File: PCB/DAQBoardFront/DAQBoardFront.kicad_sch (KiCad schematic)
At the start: 42 parts, among them IC2 LMR51430YDDCR, J2 53375-0410, U5 TCAN1051VDRQ1

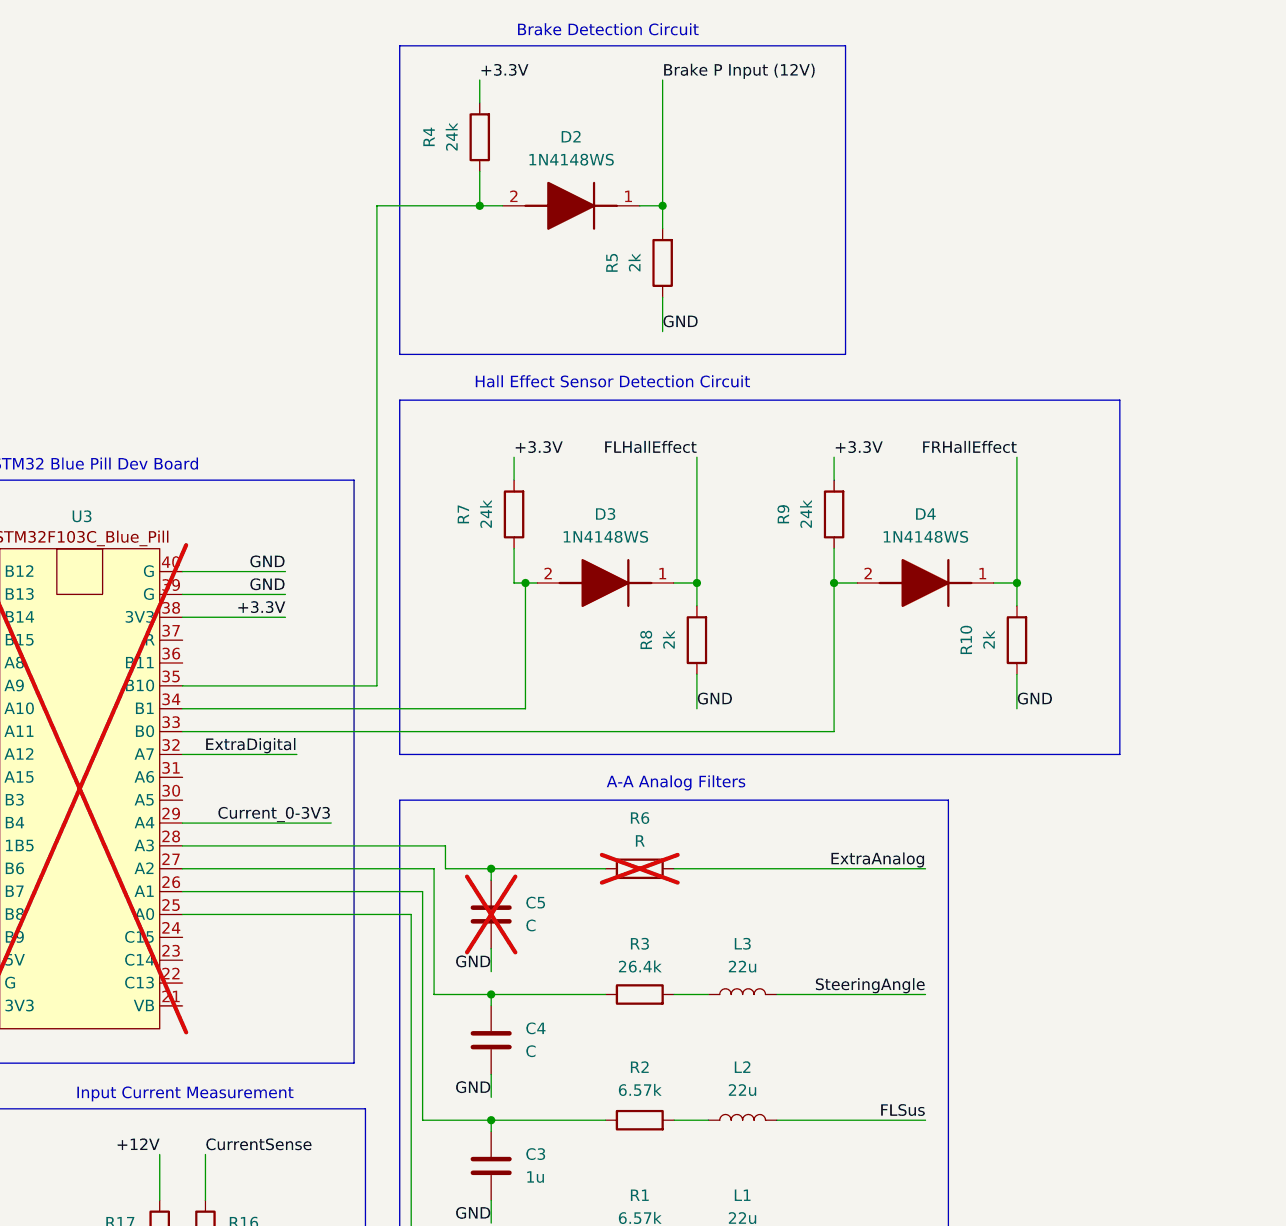
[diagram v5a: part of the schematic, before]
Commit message: Created hall effect test script for T4.1, adjusted hall effect input strategy
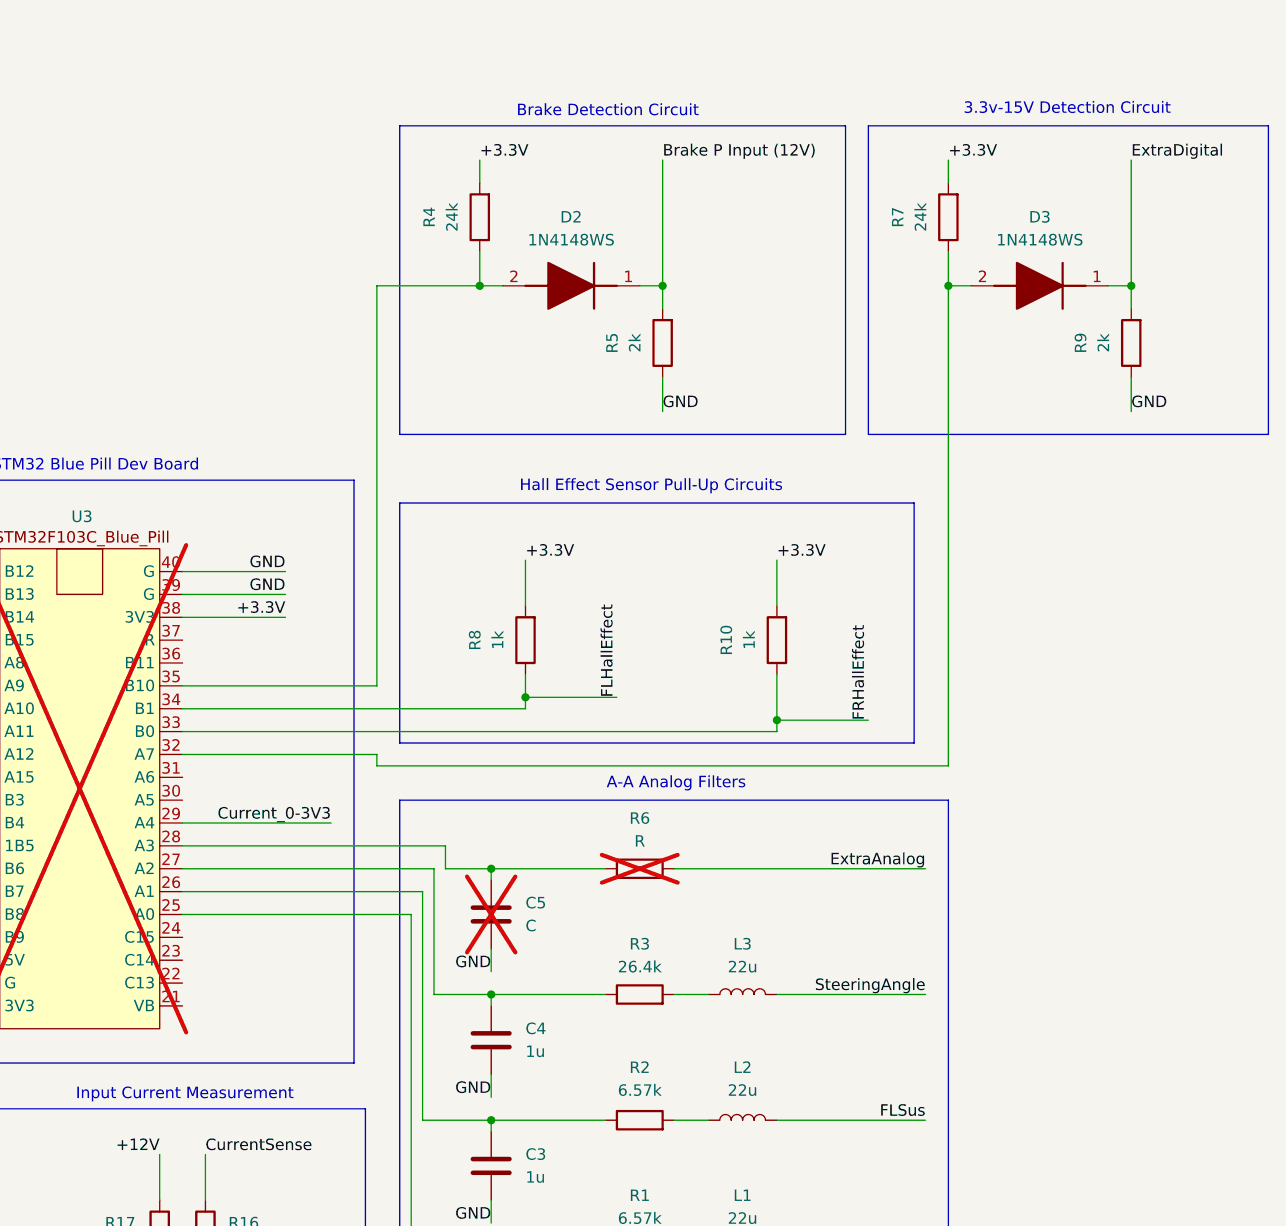
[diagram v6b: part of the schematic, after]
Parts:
- removed D4: 1N4148WS, SODFL2512X90N, symbol CFR-Symbol-Library:1N4148WS
- C4: value C -> 1u
- R10, R8: value 2k -> 1k
- R9: value 24k -> 2k; footprint LED_SMD:LED_0603_1608Metric_Pad1.05x0.95mm_HandSolder -> Resistor_SMD:R_0603_1608Metric_Pad0.98x0.95mm_HandSolder
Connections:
- net +3.3V: now also R10.2, R8.2; no longer R9.2
- net ExtraDigital: now also D3.1 (K), R9.2; no longer U3.32 (A7)
- net FLHallEffect: now also R8.1, U3.34 (B1); no longer D3.1 (K), R8.2
- net FRHallEffect: now also R10.1, U3.33 (B0); no longer R10.2
- net GND: now also R9.1; no longer R10.1, R8.1
- net at D3.2 (A), R7.1: now also U3.32 (A7); no longer U3.34 (B1)
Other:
- note added: "3.3v-15V Detection Circuit"
- note added: "Hall Effect Sensor Pull-Up Circuits"
- note removed: "Hall Effect Sensor Detection Circuit"
- moved on the sheet: D2, R10, R4, R5, R8

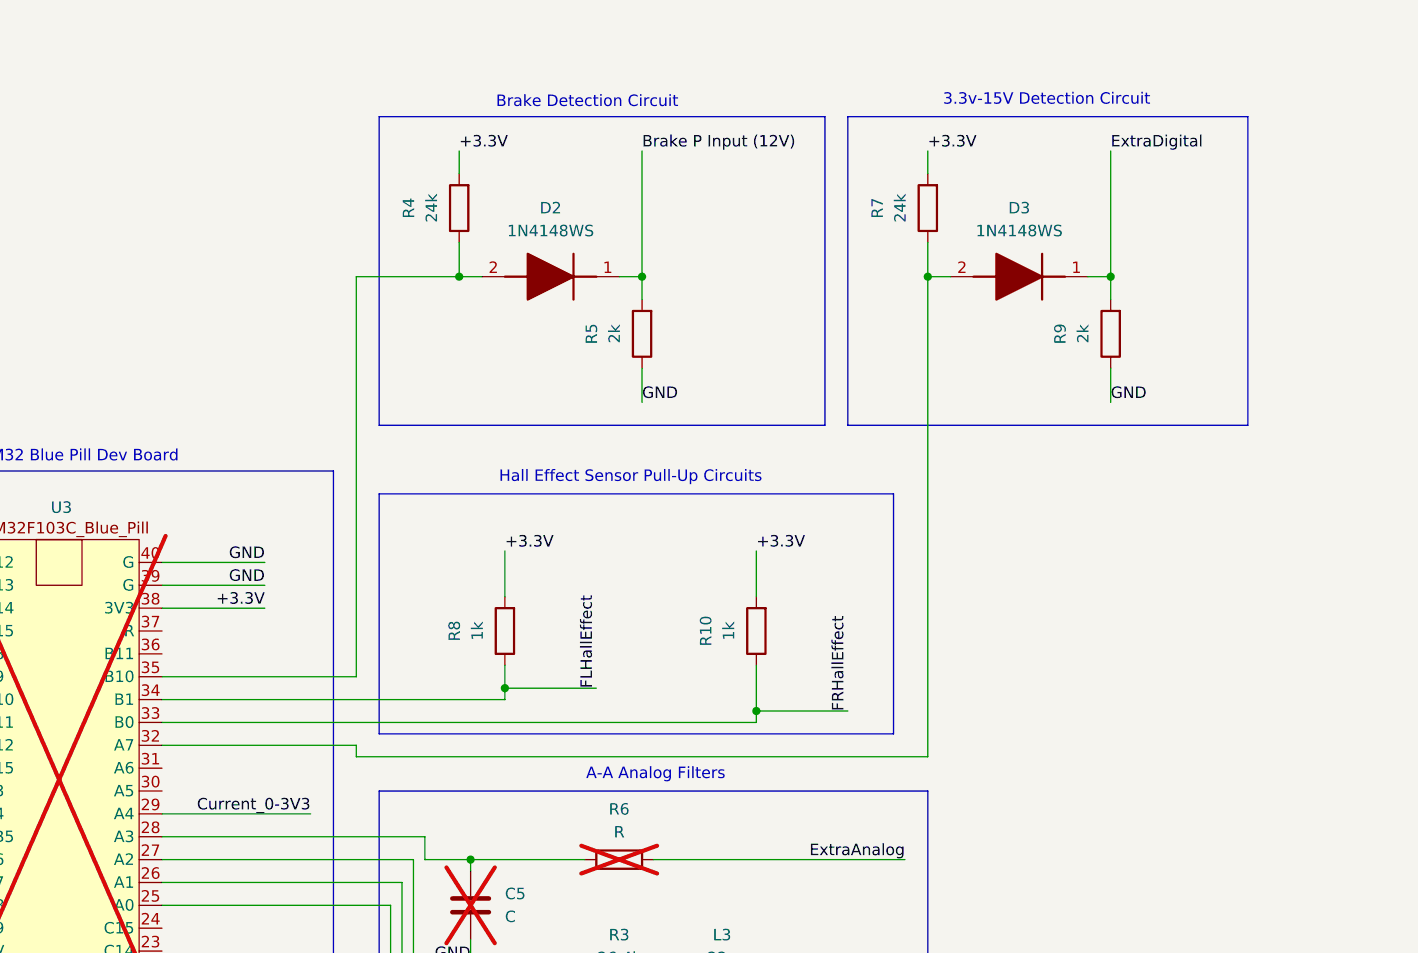
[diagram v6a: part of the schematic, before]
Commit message: Added status LEDs to the DAQ board
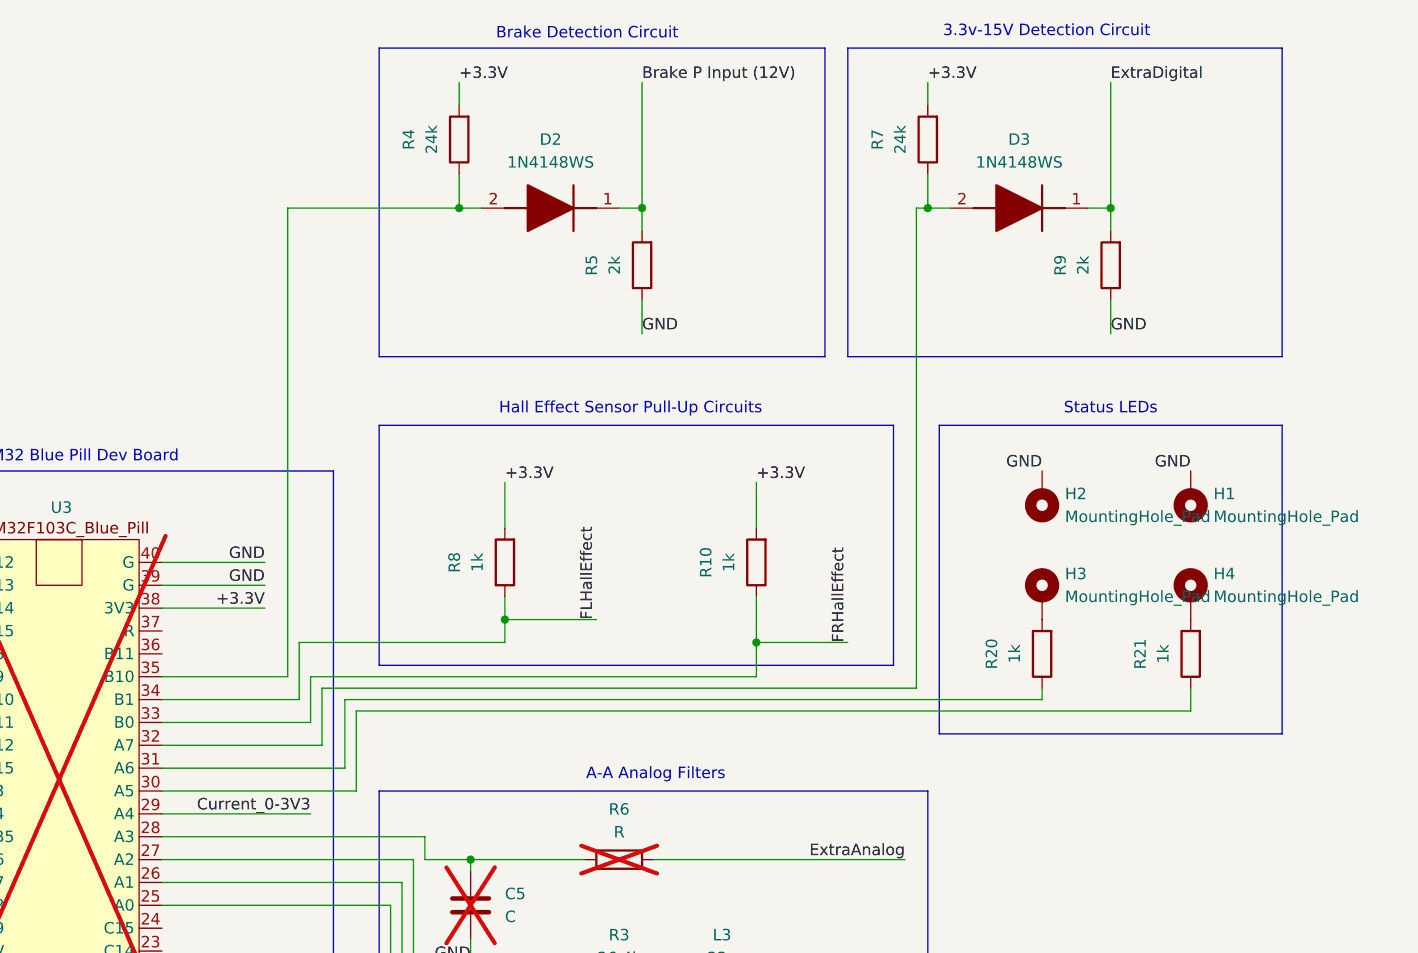
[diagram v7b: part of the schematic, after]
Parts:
- added H1, H2, H3, H4: MountingHole_Pad, Connector_PinHeader_1.00mm:PinHeader_1x01_P1.00mm_Vertical, symbol Mechanical:MountingHole_Pad
- added R20, R21: 1k, Resistor_SMD:R_0603_1608Metric_Pad0.98x0.95mm_HandSolder, symbol Device:R
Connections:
- net GND: now also H1.1, H2.1
- net at U3.30 (A5): now also R21.1
- net at U3.31 (A6): now also R20.1
- new net: H3.1, R20.2
- new net: H4.1, R21.2
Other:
- note added: "Status LEDs"
- moved on the sheet: D2, D3, R10, R4, R5, R7, R8, R9
